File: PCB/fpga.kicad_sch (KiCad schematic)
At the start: 35 parts, among them U4 XC7A100T-FTG256, Y2 ECS-3953M-400-BN-TR

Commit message: Flash
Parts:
- added IC1: S25FL256LAGMFI003, SOIC127P1030X265-16N, symbol S25FL256LAGMFI003:S25FL256LAGMFI003
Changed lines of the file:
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@@
+    )
+  )
+  (symbol (lib_id "S25FL256LAGMFI003:S25FL256LAGMFI003") (at 21.59 48.26 0) (unit 1)
+    (in_bom yes) (on_board yes) (dnp no) (fields_autoplaced)
+    (property "Reference" "IC1" (at 44.45 40.64 0)
+      (effects (font (size 1.27 1.27)))
+    )
+    (property "Value" "S25FL256LAGMFI003" (at 44.45 43.18 0)
+      (effects (font (size 1.27 1.27)))
+    )
+    (property "Footprint" "SOIC127P1030X265-16N" (at 63.5 143.18 0)
+      (effects (font (size 1.27 1.27)) (justify left top) hide)
+    )
+    (property "Datasheet" "http://www.cypress.com/file/316171/download" (at 63.5 243.18 0)
+      (effects (font (size 1.27 1.27)) (justify left top) hide)
+    )
+    (property "Height" "2.65" (at 63.5 443.18 0)
+      (effects (font (size 1.27 1.27)) (justify left top) hide)
+    )
+    (property "Manufacturer_Name" "Cypress Semiconductor" (at 63.5 543.18 0)
+      (effects (font (size 1.27 1.27)) (justify left top) hide)
+    )
+    (property "Manufacturer_Part_Number" "S25FL256LAGMFI003" (at 63.5 643.18 0)
+      (effects (font (size 1.27 1.27)) (justify left top) hide)
+    )
+    (property "Mouser Part Number" "727-S25FL256LAGMFI03" (at 63.5 743.18 0)
+      (effects (font (size 1.27 1.27)) (justify left top) hide)
+    )
+    (property "Mouser Price/Stock" "https://www.mouser.co.uk/ProductDetail/Cypress-Semiconductor/S25FL256LAGMFI003?qs=JseWDPAoSPYBUrLEMYi29A%3D%3D" (at 63.5 843.18 0)
+      (effects (font (size 1.27 1.27)) (justify left top) hide)
+    )
+    (property "Arrow Part Number" "S25FL256LAGMFI003" (at 63.5 943.18 0)
+      (effects (font (size 1.27 1.27)) (justify left top) hide)
+    )
+    (property "Arrow Price/Stock" "https://www.arrow.com/en/products/s25fl256lagmfi003/cypress-semiconductor" (at 63.5 1043.18 0)
+      (effects (font (size 1.27 1.27)) (justify left top) hide)
+    )
+    (pin "1")
+    (pin "10")
+    (pin "11")
+    (pin "12")
+    (pin "13")
+    (pin "14")
+    (pin "15")
+    (pin "16")
+    (pin "2")
+    (pin "3")
+    (pin "4")
+    (pin "5")
+    (pin "6")
+    (pin "7")
+    (pin "8")
+    (pin "9")
+    (instances
+      (project "PCB"
+        (path "/aa113cd6-c3ac-4890-9a84-1ea195994408/e43e14ef-0971-4dbf-9758-48ad88cea06a"
+          (reference "IC1") (unit 1)
+        )
+      )
     )
   )

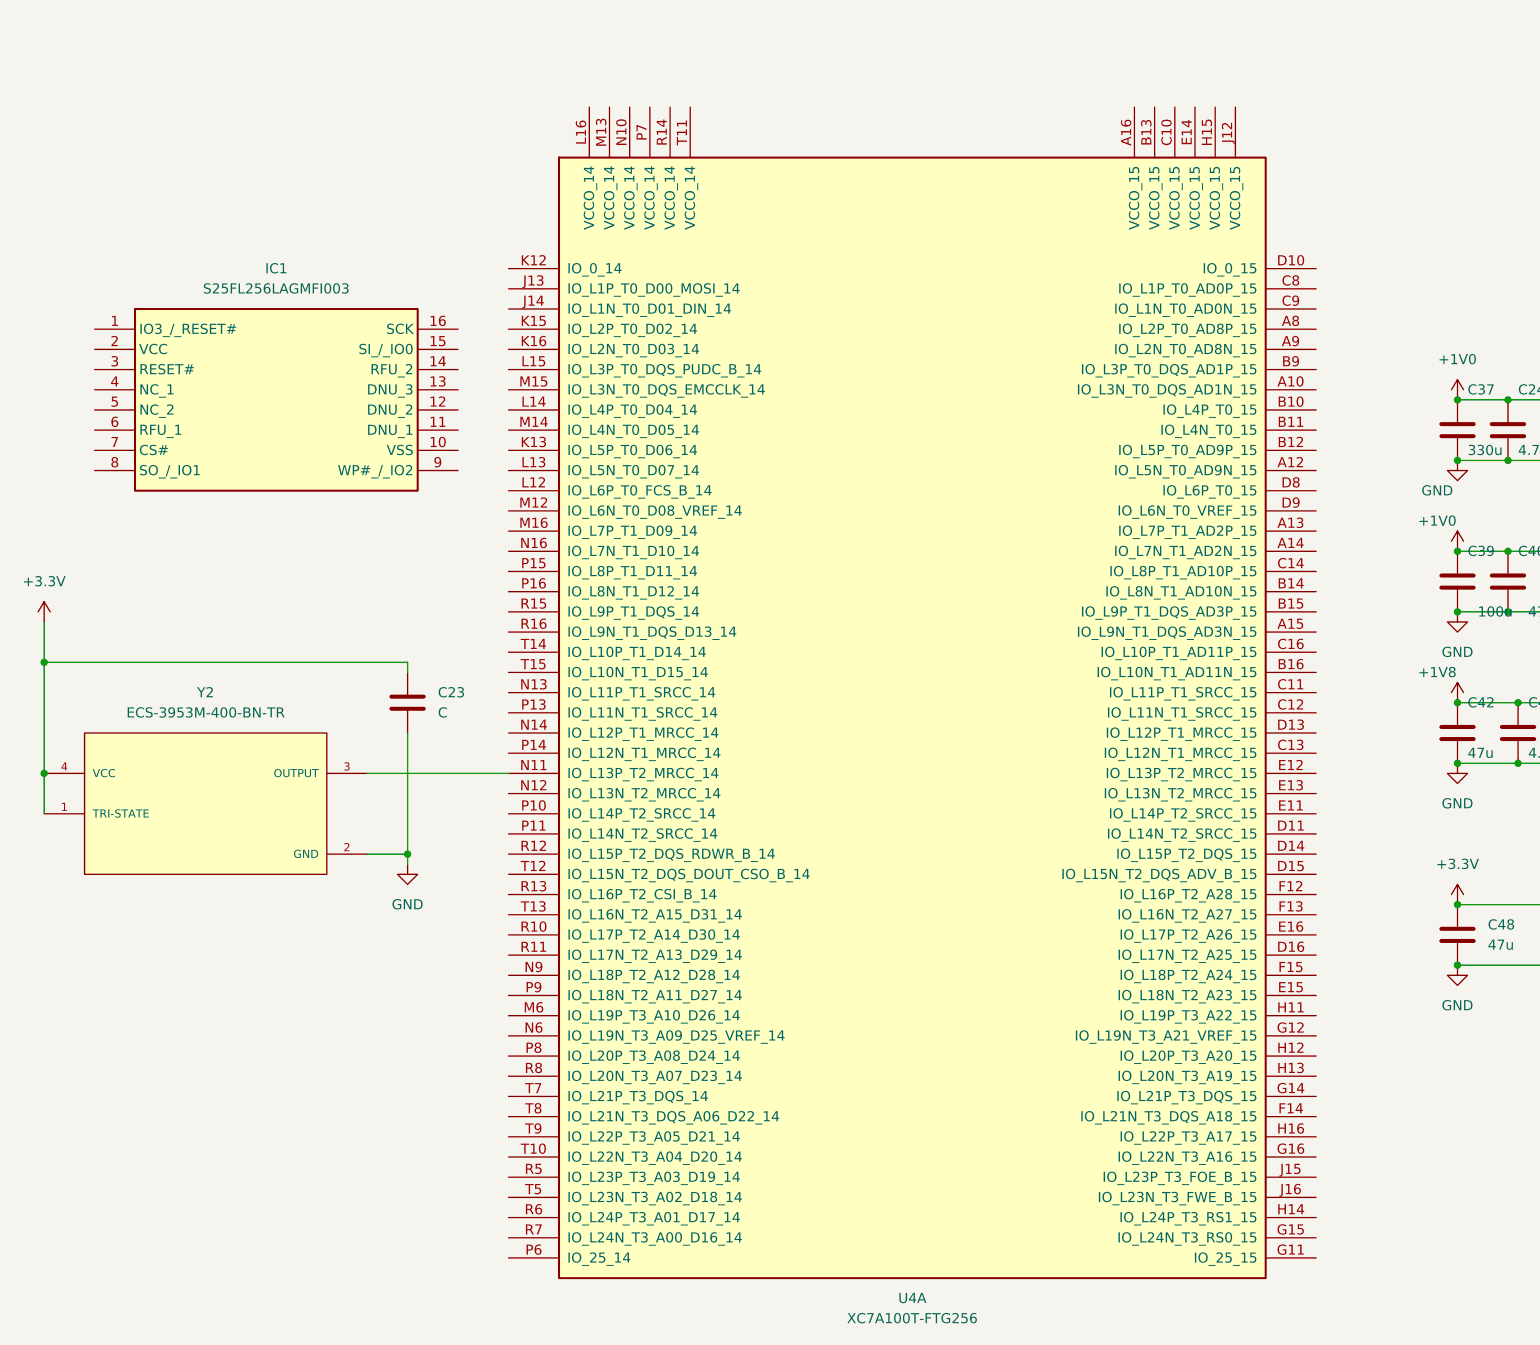
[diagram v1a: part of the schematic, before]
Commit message: FPGA - Lagt til Flash
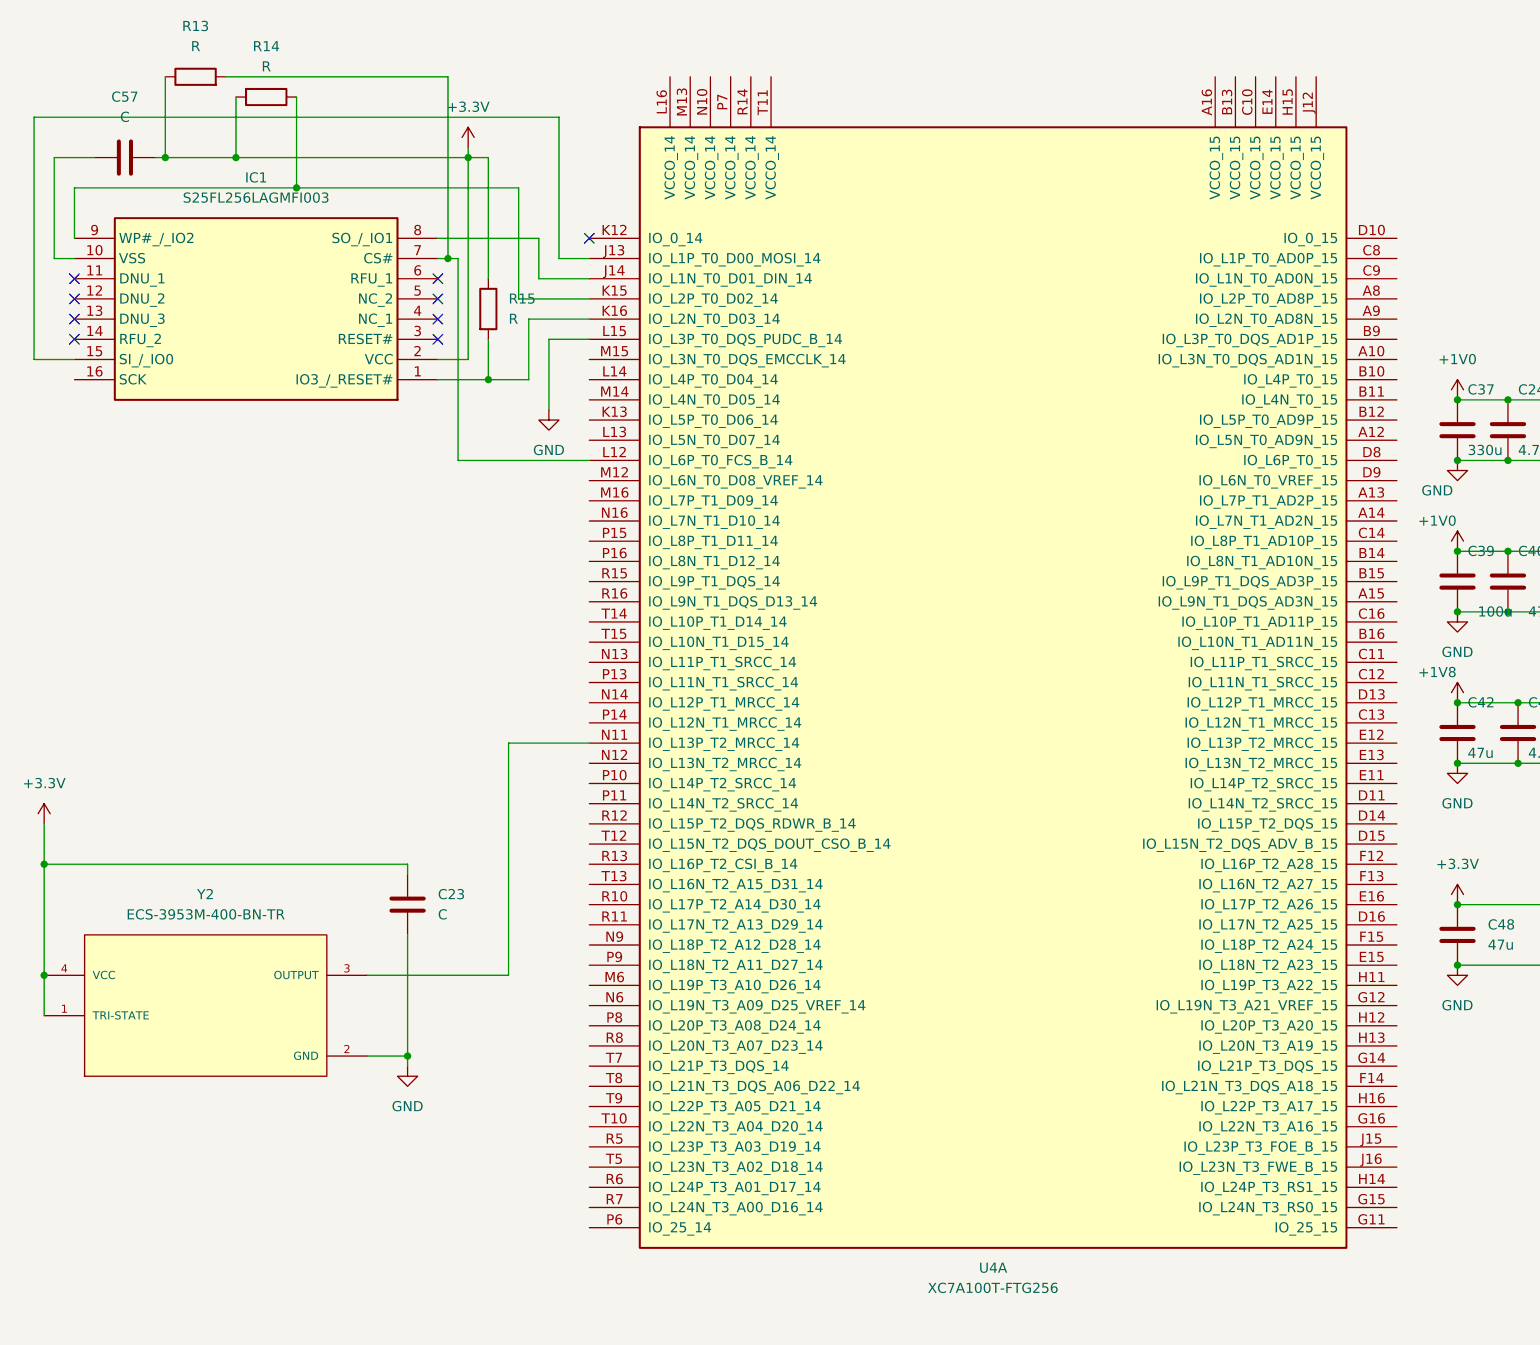
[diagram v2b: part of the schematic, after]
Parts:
- added C57: C, symbol Device:C
- added R13, R14, R15: R, symbol Device:R
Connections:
- net +3.3V: now also IC1.2 (VCC), C57.2, R13.1, R14.2, R15.1
- net GND: now also U4.L15 (IO_L3P_T0_DQS_PUDC_B_14)
- net at U4.J13 (IO_L1P_T0_D00_MOSI_14): now also IC1.15 (SI_/_IO0)
- net at U4.J14 (IO_L1N_T0_D01_DIN_14): now also IC1.8 (SO_/_IO1)
- net at U4.K15 (IO_L2P_T0_D02_14): now also IC1.9 (WP#_/_IO2), R14.1
- net at U4.K16 (IO_L2N_T0_D03_14): now also IC1.1 (IO3_/_RESET#), R15.2
- net at U4.L12 (IO_L6P_T0_FCS_B_14): now also IC1.7 (CS#), R13.2
- net at IC1.10 (VSS): now also C57.1
- no-connect marks 0 -> 9
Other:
- moved on the sheet: C23, IC1, U4A, Y2

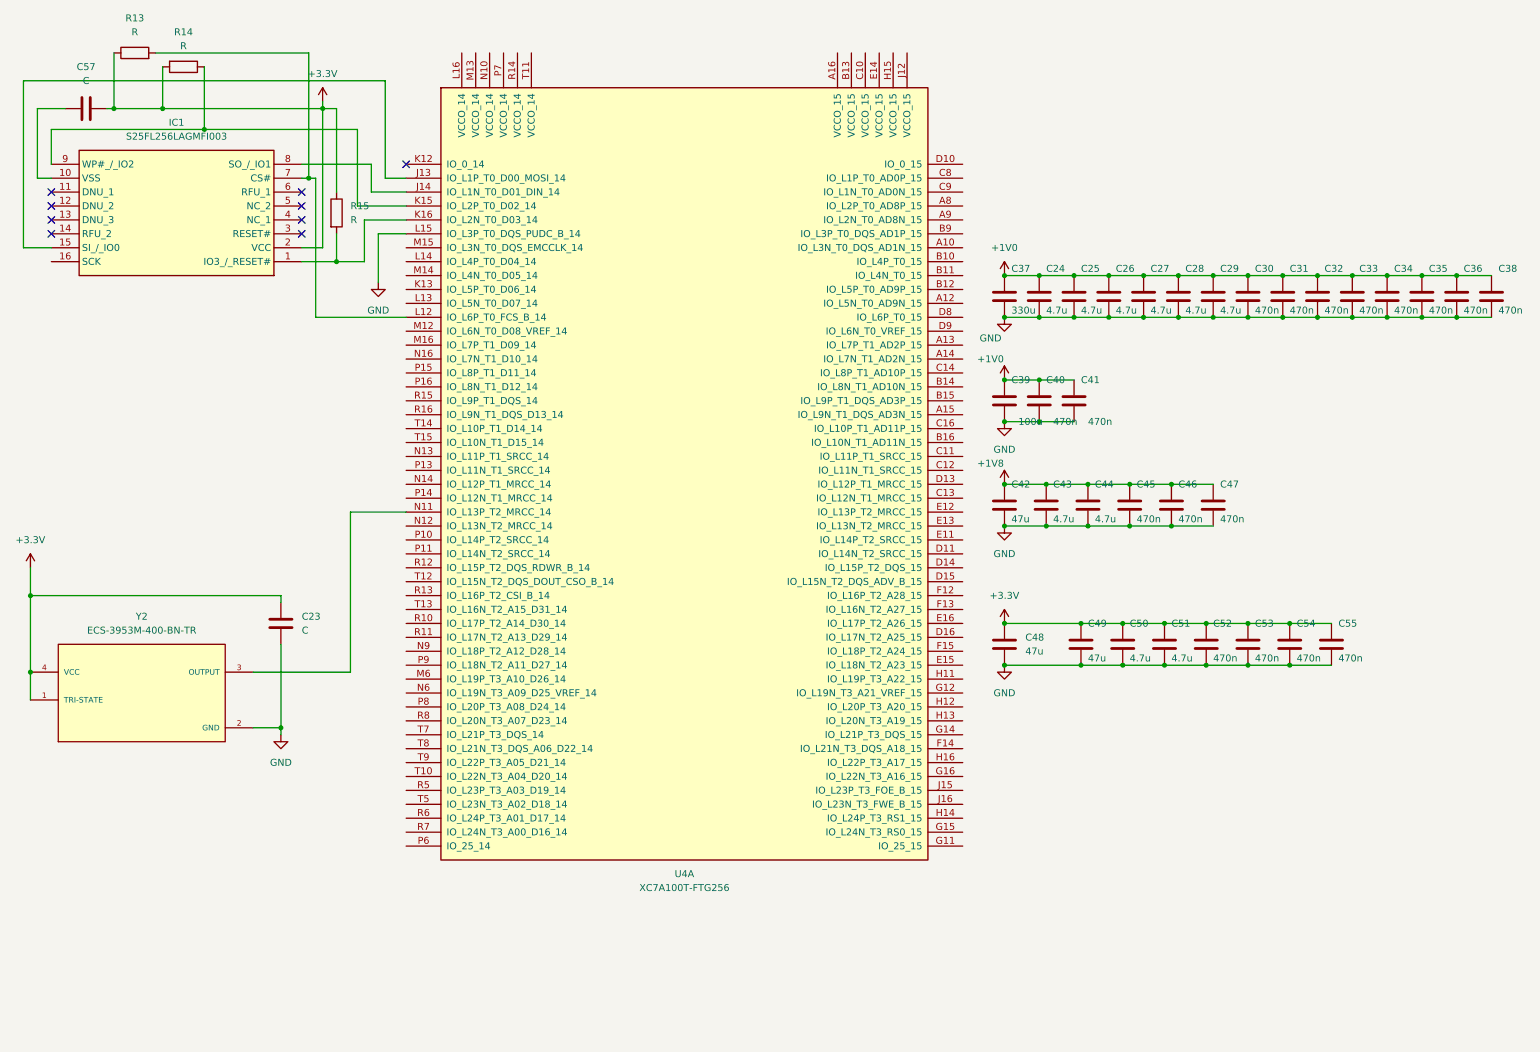
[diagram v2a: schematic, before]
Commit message: Adding unit C and D to FPGA (Stil missing unit B)
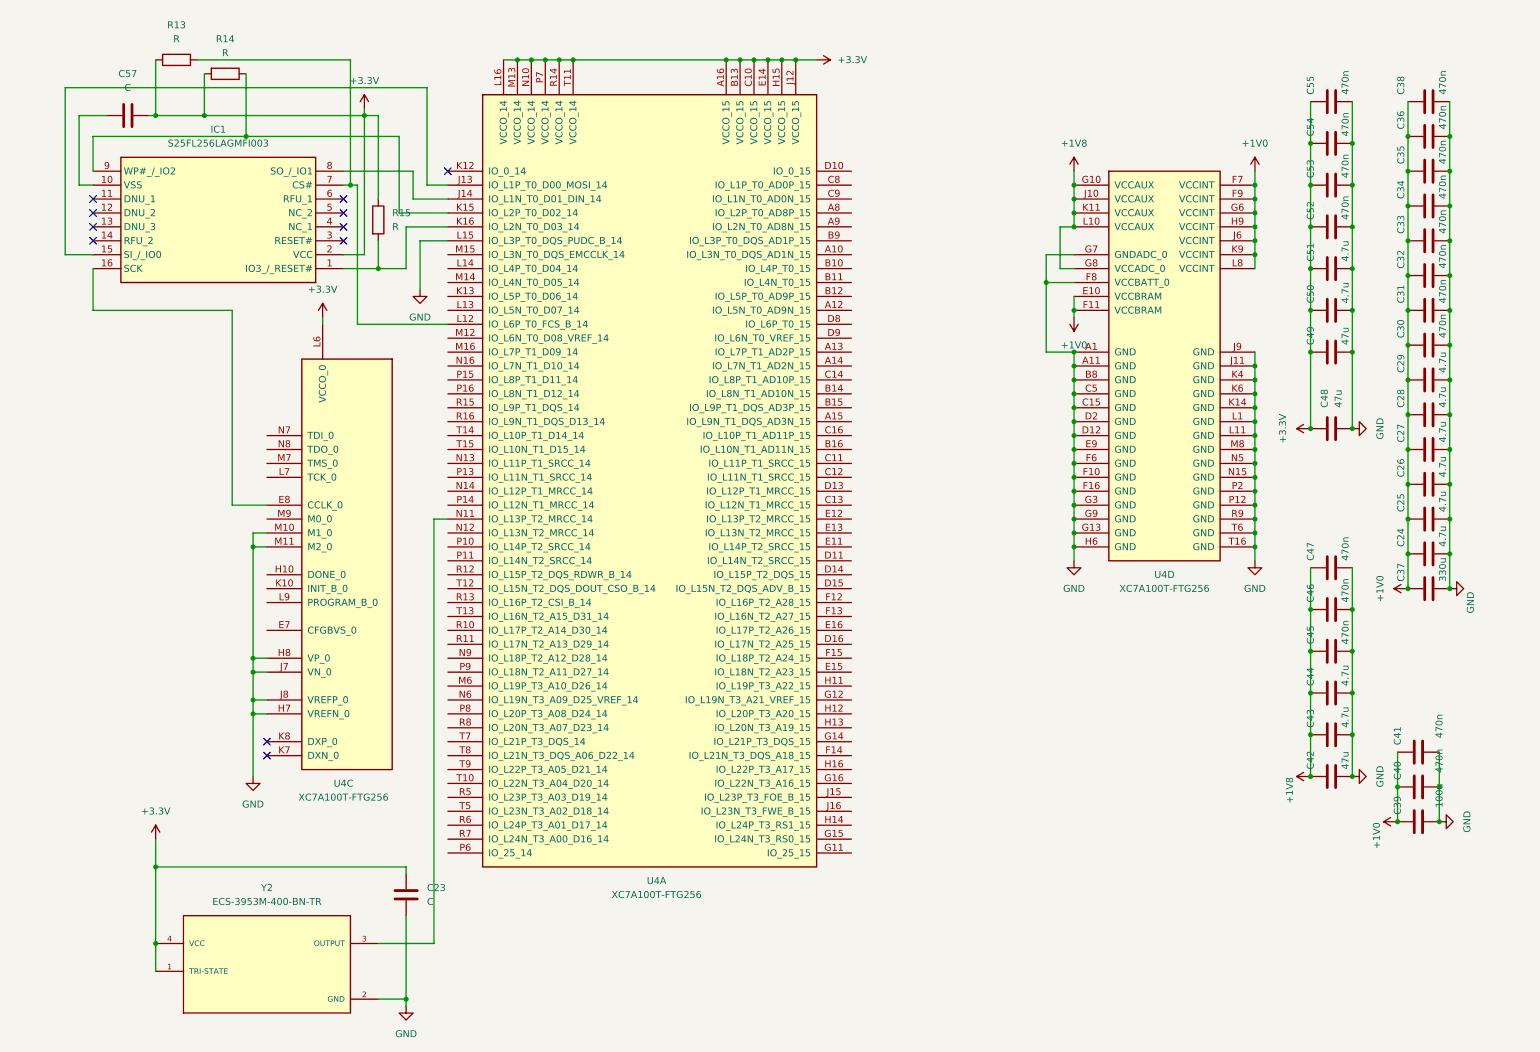
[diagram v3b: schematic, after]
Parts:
- added unit 4 of U4
- added unit 3 of U4
- IC1: footprint SOIC127P1030X265-16N -> (none)
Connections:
- net +1V0: now also U4.E10 (VCCBRAM), U4.F11 (VCCBRAM), U4.F7 (VCCINT), U4.F9 (VCCINT), U4.G6 (VCCINT), U4.H9 (VCCINT), U4.J6 (VCCINT), U4.K9 (VCCINT), U4.L8 (VCCINT)
- net +1V8: now also U4.G10 (VCCAUX), U4.G8 (VCCADC_0), U4.J10 (VCCAUX), U4.K11 (VCCAUX), U4.L10 (VCCAUX)
- net +3.3V: now also U4.A16 (VCCO_15), U4.B13 (VCCO_15), U4.C10 (VCCO_15), U4.E14 (VCCO_15), U4.H15 (VCCO_15), U4.J12 (VCCO_15), U4.L16 (VCCO_14), U4.M13 (VCCO_14), U4.N10 (VCCO_14), U4.P7 (VCCO_14), U4.R14 (VCCO_14), U4.T11 (VCCO_14), U4.L6 (VCCO_0)
- net GND: now also U4.A1 (GND), U4.A11 (GND), U4.B8 (GND), U4.C15 (GND), U4.C5 (GND), U4.D12 (GND), U4.D2 (GND), U4.E9 (GND), U4.F10 (GND), U4.F16 (GND), U4.F6 (GND), U4.F8 (VCCBATT_0), U4.G13 (GND), U4.G3 (GND), U4.G7 (GNDADC_0), U4.G9 (GND), U4.H6 (GND), U4.H7 (VREFN_0), U4.H8 (VP_0), U4.J11 (GND), U4.J7 (VN_0), U4.J8 (VREFP_0), U4.J9 (GND), U4.K14 (GND), U4.K4 (GND), U4.K6 (GND), U4.L1 (GND), U4.L11 (GND), U4.M10 (M1_0), U4.M11 (M2_0), U4.M8 (GND), U4.N15 (GND), U4.N5 (GND), U4.P12 (GND), U4.P2 (GND), U4.R9 (GND), U4.T16 (GND), U4.T6 (GND)
- net at IC1.16 (SCK): now also U4.E8 (CCLK_0)
- no-connect marks 9 -> 11
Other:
- moved on the sheet: C23, C24, C25, C26, C27, C28, C29, C30, C31, C32, C33, C34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

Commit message: Debugg added, missing one unit still
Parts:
- added J1: 0878311420, 0878311420, symbol 0878311420:0878311420
- added R16, R17, R18, R19, R20: R, symbol Device:R
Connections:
- net GND: now also J1.1, J1.11, J1.13, J1.3, J1.5, J1.7, J1.9
- net +3V3: now reaches U4.E7 (CFGBVS_0)
- net +3V3: now also U4.M9 (M0_0), J1.2, R16.1, R17.2, R18.2, R19.2, R20.1
- net done: now reaches U4.H10 (DONE_0)
- net done: now also R20.2
- net at U4.K10 (INIT_B_0): now also R18.1
- net at U4.L7 (TCK_0): now also J1.6
- net program_b: now reaches U4.L9 (PROGRAM_B_0)
- net program_b: now also R19.1
- net at U4.M7 (TMS_0): now also J1.4, R16.2, R17.1
- net at U4.N7 (TDI_0): now also J1.10
- net at U4.N8 (TDO_0): now also J1.8
- no-connect marks 11 -> 13
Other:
- moved on the sheet: C23, C57, IC1, R13, R14, R15, U4A, U4C, Y2

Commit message: Work
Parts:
- added unit 2 of U4
- added U5: IS62C1024AL-35QLI-TR, IS62C1024AL-35QLI-TR:SOIC127P1412X305-32N, symbol IS62C1024AL-35QLI-TR:IS62C1024AL-35QLI-TR
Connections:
- net +3.3V: now also U5.32 (VDD)
- net GND: now also U5.16 (GND)
- net at U4.C11 (IO_L11P_T1_SRCC_15): now also U5.2 (A16)
- net at U4.C12 (IO_L11N_T1_SRCC_15): now also U5.31 (A15)
- net at U4.C13 (IO_L12N_T1_MRCC_15): now also U5.3 (A14)
- net at U4.D11 (IO_L14N_T2_SRCC_15): now also U5.26 (A9)
- net at U4.D13 (IO_L12P_T1_MRCC_15): now also U5.28 (A13)
- net at U4.D14 (IO_L15P_T2_DQS_15): now also U5.27 (A8)
- net at U4.D15 (IO_L15N_T2_DQS_ADV_B_15): now also U5.5 (A7)
- net at U4.D16 (IO_L17N_T2_A25_15): now also U5.9 (A3)
- net at U4.E11 (IO_L14P_T2_SRCC_15): now also U5.23 (A10)
- net at U4.E12 (IO_L13P_T2_MRCC_15): now also U5.4 (A12)
- net at U4.E13 (IO_L13N_T2_MRCC_15): now also U5.25 (A11)
- net at U4.E15 (IO_L18N_T2_A23_15): now also U5.11 (A1)
- net at U4.E16 (IO_L17P_T2_A26_15): now also U5.8 (A4)
- net at U4.F12 (IO_L16P_T2_A28_15): now also U5.6 (A6)
- net at U4.F13 (IO_L16N_T2_A27_15): now also U5.7 (A5)
- net at U4.F14 (IO_L21N_T3_DQS_A18_15): now also U5.13 (I/O0)
- net at U4.F15 (IO_L18P_T2_A24_15): now also U5.10 (A2)
- net at U4.G11 (IO_25_15): now also U5.21 (I/O7)
- net at U4.G12 (IO_L19N_T3_A21_VREF_15): now also U5.29 (~WE)
- net at U4.G14 (IO_L21P_T3_DQS_15): now also U5.22 (~CE1)
- net at U4.G15 (IO_L24N_T3_RS0_15): now also U5.20 (I/O6)
- net at U4.G16 (IO_L22N_T3_A16_15): now also U5.15 (I/O2)
- net at U4.H11 (IO_L19P_T3_A22_15): now also U5.12 (A0)
- net at U4.H12 (IO_L20P_T3_A20_15): now also U5.24 (~OE)
- net at U4.H13 (IO_L20N_T3_A19_15): now also U5.30 (CE2)
- net at U4.H14 (IO_L24P_T3_RS1_15): now also U5.19 (I/O5)
- net at U4.H16 (IO_L22P_T3_A17_15): now also U5.14 (I/O1)
- net at U4.J15 (IO_L23P_T3_FOE_B_15): now also U5.17 (I/O3)
- net at U4.J16 (IO_L23N_T3_FWE_B_15): now also U5.18 (I/O4)
- net at IC1.1 (IO3_/_RESET#), R15.2: no longer U4.K16 (IO_L2N_T0_D03_14)
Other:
- moved on the sheet: C24, C25, C26, C27, C28, C29, C30, C31, C32, C33, C34, C35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
